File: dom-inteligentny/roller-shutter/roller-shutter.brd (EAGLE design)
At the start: 64 x 84 mm, 19 parts, among them K1 RP421110, K2 691218410003, K3 691218410003, K4 RP421110, Q1 16MHz, T1 BC847, T2 BC847, U1 ATMEGA328

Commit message: Roller shutter
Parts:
- removed K2, K3: 691218410003, Wurth_Elektronik_Electromechanic_Terminal_Blocks_Connectors_rev15c:691218410003
- added C3, C7: (no value), eagle-ltspice:C0805
- added C8, C9: (no value), eagle-ltspice:C1812
- added JP2: (no value), pinhead:1X03
- added R4, R5: (no value), eagle-ltspice:R1206
- added R6, R7: (no value), eagle-ltspice:R2512
- added X1, X4: (no value), con-ptr500:AK500/3
- added X2, X3: JST-XH-05-PIN-LONG-PAD, Rembrandt Electronics - JST XH Connectors v1-0:JST-XH-05-PACKAGE-LONG-PAD
- moved JP1 14.2 mm to (39.7, 26.7)
- moved K4 14.2 mm to (23.5, 41.1)
- moved R2 14.2 mm to (29.7, 31.5)
- moved D2 14.2 mm to (27.2, 33.8)
- moved R3 14.2 mm to (17.9, 29.2)
- moved C1 14.2 mm to (17.4, 13.0)
- moved C2 14.2 mm to (22.3, 16.0)
- moved U1 14.2 mm to (27.8, 22.6)
- moved D1 14.2 mm to (39.3, 33.5)
- moved K1 14.2 mm to (37.2, 41.1)
- moved R1 14.2 mm to (19.8, 20.8)
- moved T1 14.2 mm to (35.5, 32.4)
- moved T2 14.2 mm to (20.7, 31.7)
- moved C6 14.2 mm to (27.6, 29.1)
- moved Q1 13.7 mm to (38.5, 17.4)
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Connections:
- new net N$10: C9.2, R6.1
- new net N$9: C8.2, R7.1
- net A2: now also C7.2, R5.1, X4.3
- net A3: now also C3.2, R4.1, X4.2
- net A4: now also X2.2, X3.2
- net A5: now also X2.1, X3.1
- net GND: now also C3.1, C7.1, X2.4, X2.5, X3.4, X3.5, X4.1
- net N$1: now also JP2.1
- net N$2: now also JP2.2
- net N$4: now also C8.1, C9.1, X1.1; no longer K3.1
- net N$7: now also R7.2, X1.3; no longer K3.3
- net N$8: now also R6.2, X1.2; no longer K3.2
- net VCC: now also JP2.3, R4.2, R5.2, X2.3, X3.3
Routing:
- net GND: track 98.7 -> 218.7 mm, vias 3 -> 4
- net VCC: track 61.9 -> 176.9 mm, vias 0 -> 1
- net A3: track 0.00 -> 79.1 mm
- net A2: track 0.00 -> 73.3 mm
- net N$4: track 46.7 -> 98.5 mm
- net A4: track 0.00 -> 47.6 mm, vias 0 -> 1
- net A5: track 0.00 -> 44.7 mm, vias 0 -> 2
- net N$7: track 18.0 -> 61.4 mm
- net N$8: track 19.3 -> 44.2 mm
- net N$1: track 11.6 -> 32.7 mm
- net N$2: track 10.3 -> 20.9 mm
- net N$9: track 0.00 -> 2.49 mm
- net N$10: track 0.00 -> 2.36 mm
- net N$44: track 17.0 -> 18.3 mm
- net N$43: track 12.7 -> 12.1 mm
- added copper zone on layer 1, net GND
- added copper zone on layer 16, net GND
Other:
- board size 64 x 84 mm -> 48.5 x 84 mm
- board text added: "5V"
- board text added: "Falcon IoT Roller Shutter v1.0 weblogic.pl falcon.software"
- board text added: "GND"
- board text added: "SCL"
- board text added: "SDA"
- board text added: "VCC"

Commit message: roller shutter
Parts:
- added JP6: (no value), pinhead-zmiany-JP:3X04
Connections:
- net D10: now also JP6.2
- net D7: now also JP6.11
- net D8: now also JP6.8
- net D9: now also JP6.5
- net GND: now also JP6.12, JP6.3, JP6.6, JP6.9
- net VCC: now also JP6.1, JP6.10, JP6.4, JP6.7
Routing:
- net D10: track 0.00 -> 41.2 mm, vias 0 -> 1
- net D9: track 0.00 -> 40.7 mm, vias 0 -> 1
- net D8: track 0.00 -> 38.3 mm, vias 0 -> 1
- net D7: track 0.00 -> 36.1 mm, vias 0 -> 1
- net VCC: track 176.9 -> 207.0 mm
- net GND: track 218.7 -> 229.0 mm
- net A4: track 47.6 -> 46.9 mm
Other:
- board text added: "0"
- board text added: "1"

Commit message: Roller shutter ark change
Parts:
- removed X1: (no value), con-ptr500:AK500/3
- added X5: (no value), con-ptr500:AK500/4
- moved C8 4.62 mm to (35.9, 67.3)
- moved R7 4.62 mm to (43.2, 67.3)
- moved C9 4.36 mm to (29.3, 67.3)
- moved R6 4.24 mm to (22.1, 67.3)
- moved X4 1.52 mm to (14.4, 79.9)
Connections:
- new net N$11: C8.1, C9.1, X5.2
- net N$4: now also X5.1; no longer C8.1, C9.1, X1.1
- net N$7: now also X5.4; no longer X1.3
- net N$8: now also X5.3; no longer X1.2
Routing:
- net N$4: track 98.5 -> 77.2 mm
- net N$11: track 0.00 -> 14.7 mm
- net N$8: track 44.2 -> 42.1 mm
- net A2: track 73.3 -> 72.1 mm
- net GND: track 229.0 -> 228.4 mm
- net A3: track 79.1 -> 78.4 mm
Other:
- board text added: "A"
- board text added: "B"
- board text added: "G"
- board text added: "L"
- board text added: "L1"
- board text added: "L2"
- board text added: "N"

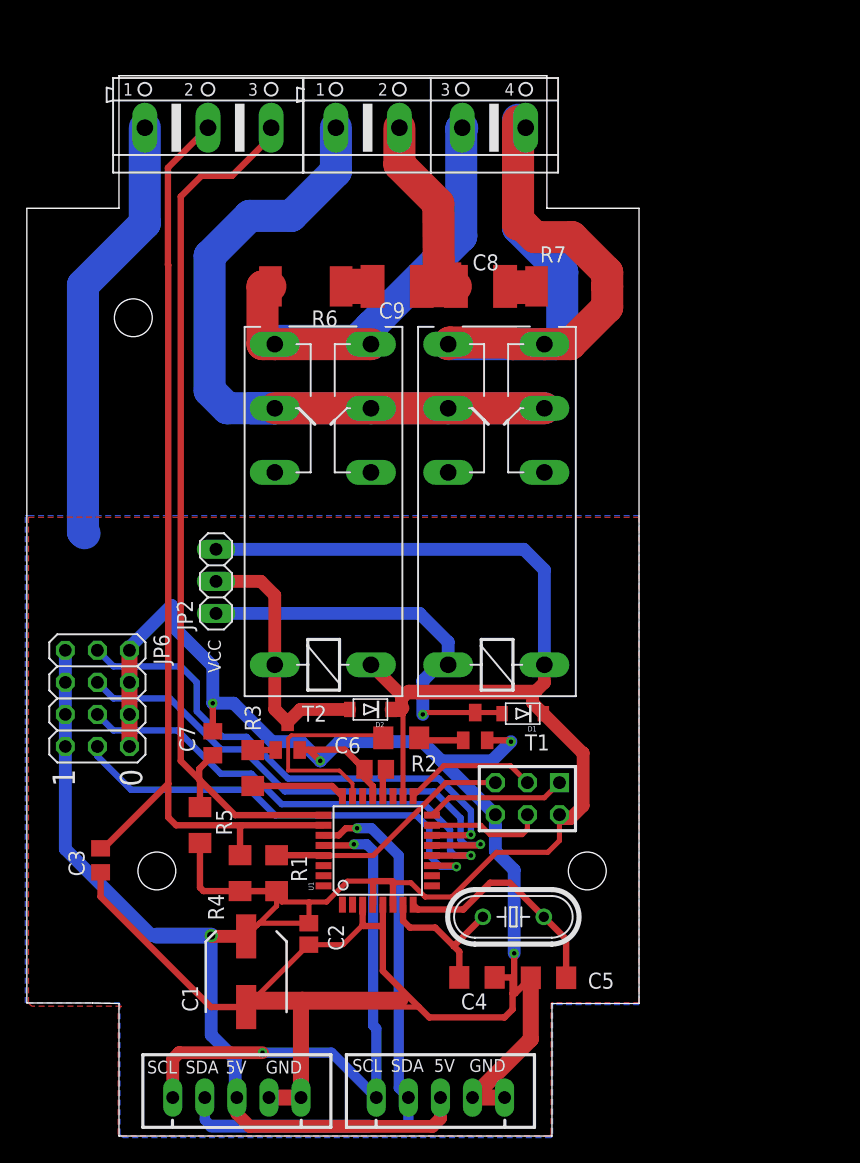
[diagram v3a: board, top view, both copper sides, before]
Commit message: Roller shutter, heat controller WIP and a new light switch input board
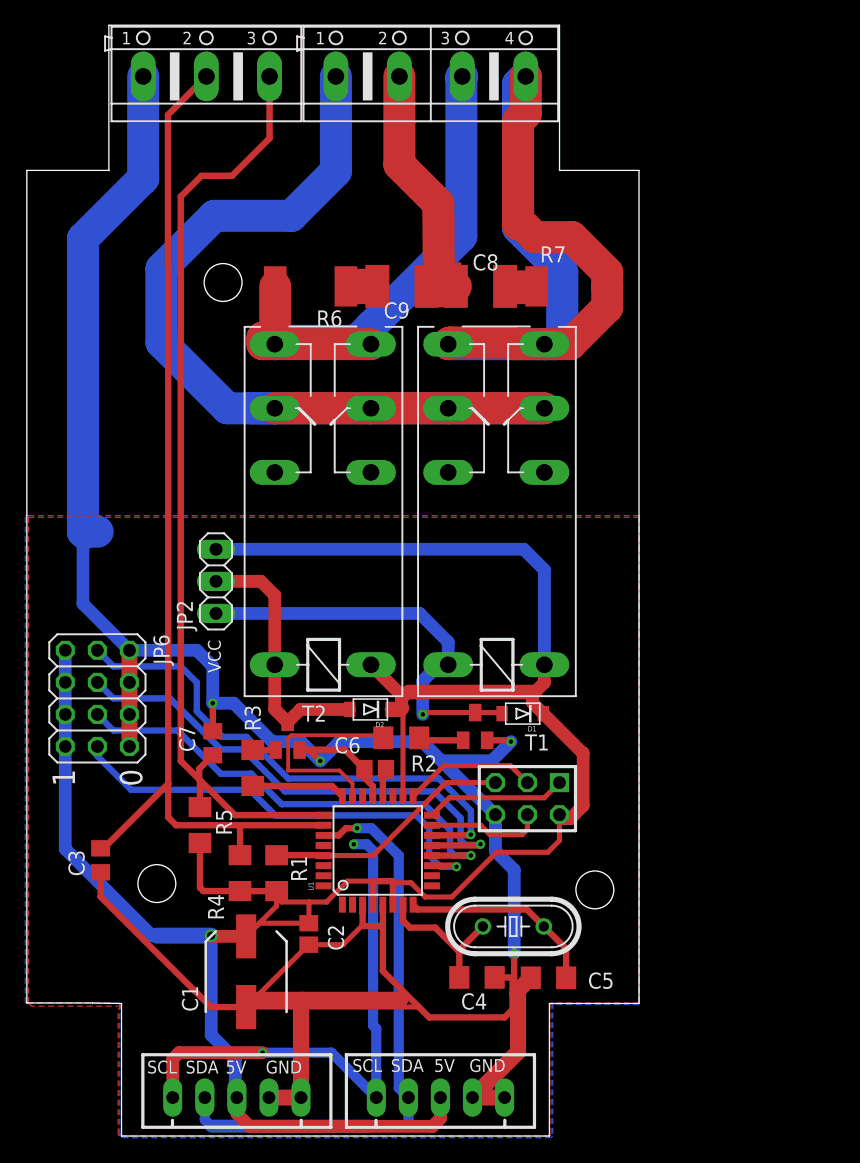
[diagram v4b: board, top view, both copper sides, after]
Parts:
- moved X4 4.07 mm to (14.2, 83.9)
- moved X5 4.06 mm to (32.0, 83.9)
- moved Q1 0.76 mm to (38.5, 16.6)
- moved C9 0.38 mm to (29.7, 67.3)
- moved R6 0.38 mm to (22.5, 67.3)
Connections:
- net A4 renamed SDA
- net A5 renamed SCL
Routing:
- net GND: track 228.4 -> 240.7 mm
- net N$4: track 77.2 -> 86.1 mm
- net N$7: track 61.6 -> 69.1 mm
- net N$8: track 42.1 -> 46.6 mm
- net N$11: track 14.7 -> 18.7 mm
- net A3: track 78.4 -> 82.4 mm
- net A2: track 72.1 -> 76.1 mm
- net SCL: track 44.7 -> 42.4 mm
- net N$44: track 18.3 -> 16.1 mm
- net N$43: track 12.1 -> 11.5 mm
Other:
- board size 48.5 x 84 mm -> 48.5 x 88 mm

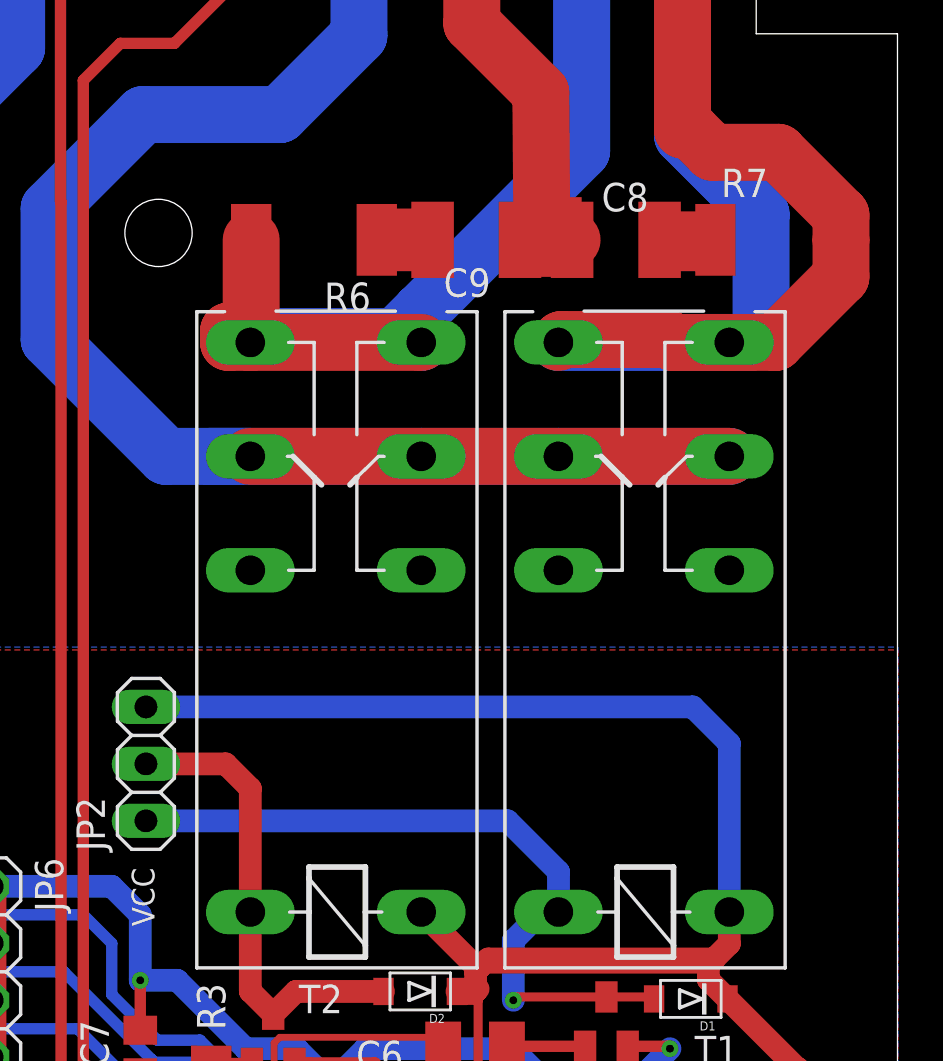
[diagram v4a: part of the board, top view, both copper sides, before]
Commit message: adds SSR to roller shutter controller
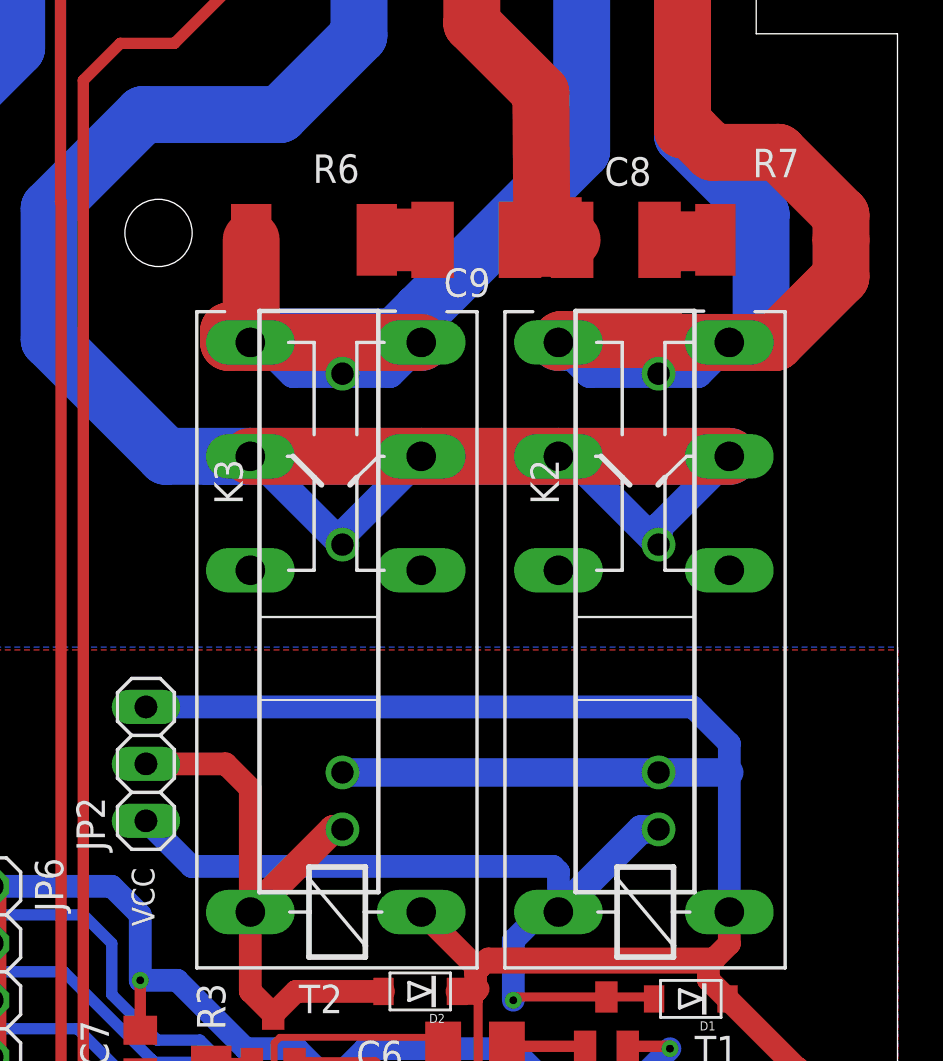
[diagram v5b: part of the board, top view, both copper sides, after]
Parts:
- added K2, K3: OMRON-G3MB-202P-SSR, Omron G3MB 202p SSR:OMRON-G3MB-202P-SSR
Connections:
- net N$1: now also K2.4
- net N$2: now also K3.4
- net N$4: now also K2.2, K3.2
- net N$7: now also K2.1
- net N$8: now also K3.1
- net VCC: now also K2.3, K3.3
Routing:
- net N$4: track 86.1 -> 108.5 mm
- net VCC: track 207.0 -> 224.3 mm
- net N$7: track 69.1 -> 77.9 mm
- net N$8: track 46.6 -> 55.2 mm
- net N$1: track 32.7 -> 38.7 mm
- net N$2: track 20.9 -> 26.6 mm
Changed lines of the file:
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@@
 <setting verticaltext="up"/>
 </settings>
-<grid distance="5" unitdist="mil" unit="mm" style="lines" multiple="1" display="no" altdistance="5" altunitdist="mil" altunit="mil"/>
+<grid distance="5" unitdist="mil" unit="mil" style="lines" multiple="1" display="no" altdistance="5" altunitdist="mil" altunit="mil"/>
 <layers>
 <layer number="1" name="Top" color="4" fill="1" visible="yes" active="yes"/>
@@
 <layer number="112" name="tSilk" color="7" fill="1" visible="yes" active="yes"/>
 <layer number="113" name="IDFDebug" color="4" fill="1" visible="yes" active="yes"/>
+<layer number="114" name="Badge_Outline" color="7" fill="1" visible="yes" active="yes"/>
+<layer number="115" name="ReferenceISLANDS" color="7" fill="1" visible="yes" active="yes"/>
 <layer number="116" name="Patch_BOT" color="9" fill="4" visible="no" active="yes"/>
 <layer number="118" name="Rect_Pads" color="7" fill="1" visible="no" active="no"/>
@@
 </element>
 <element name="R6" library="eagle-ltspice" library_urn="urn:adsk.eagle:library:217" package="R2512" package3d_urn="urn:adsk.eagle:package:13304/1" value="" x="22.479" y="67.31" smashed="yes" rot="R180">
-<attribute name="NAME" x="25.019" y="65.405" size="1.27" layer="25" rot="R180"/>
+<attribute name="NAME" x="24.511" y="71.12" size="1.27" layer="25" rot="R180"/>
 <attribute name="SPICEMODEL" value="NONE" x="22.479" y="67.31" size="1.778" layer="27" rot="R180" display="off"/>
 <attribute name="SPICEPREFIX" value="R" x="22.479" y="67.31" size="1.778" layer="27" rot="R180" display="off"/>
@@
 </element>
 <element name="R7" library="eagle-ltspice" library_urn="urn:adsk.eagle:library:217" package="R2512" package3d_urn="urn:adsk.eagle:package:13304/1" value="" x="43.18" y="67.31" smashed="yes">
-<attribute name="NAME" x="40.64" y="69.215" size="1.27" layer="25"/>
+<attribute name="NAME" x="42.037" y="70.104" size="1.27" layer="25"/>
 <attribute name="SPICEMODEL" value="NONE" x="43.18" y="67.31" size="1.778" layer="27" display="off"/>
 <attribute name="SPICEPREFIX" value="R" x="43.18" y="67.31" size="1.778" layer="27" display="off"/>
@@
 </element>
 <element name="C8" library="eagle-ltspice" library_urn="urn:adsk.eagle:library:217" package="C1812" package3d_urn="urn:adsk.eagle:package:13267/1" value="" x="35.941" y="67.31" smashed="yes">
-<attribute name="NAME" x="35.306" y="68.58" size="1.27" layer="25"/>
+<attribute name="NAME" x="35.433" y="69.723" size="1.27" layer="25"/>
 <attribute name="SPICEMODEL" value="NONE" x="35.941" y="67.31" size="1.778" layer="27" display="off"/>
 <attribute name="SPICEPREFIX" value="C" x="35.941" y="67.31" size="1.778" layer="27" display="off"/>
@@
 <attribute name="POPULARITY" value="4" x="32.004" y="83.947" size="1.778" layer="27" display="off"/>
 <attribute name="VALUE" x="21.9202" y="78.232" size="1.778" layer="27" ratio="10"/>
+</element>
+<element name="K2" library="Omron G3MB 202p SSR" package="OMRON-G3MB-202P-SSR" value="OMRON-G3MB-202P-SSR" x="37.846" y="48.641" smashed="yes" rot="R270">
+<attribute name="MF" value="" x="37.846" y="48.641" size="1.778" layer="27" rot="R270" display="off"/>
+<attribute name="MPN" value="" x="37.846" y="48.641" size="1.778" layer="27" rot="R270" display="off"/>
+<attribute name="NAME" x="32.131" y="57.531" size="1.27" layer="25" rot="R270"/>
+<attribute name="OC_FARNELL" value="" x="37.846" y="48.641" size="1.778" layer="27" rot="R270" display="off"/>
+<attribute name="OC_NEWARK" value="" x="37.846" y="48.641" size="1.778" layer="27" rot="R270" display="off"/>
+</element>
+<element name="K3" library="Omron G3MB 202p SSR" package="OMRON-G3MB-202P-SSR" value="OMRON-G3MB-202P-SSR" x="23.749" y="48.641" smashed="yes" rot="R270">
+<attribute name="MF" value="" x="23.749" y="48.641" size="1.778" layer="27" rot="R270" display="off"/>
+<attribute name="MPN" value="" x="23.749" y="48.641" size="1.778" layer="27" rot="R270" display="off"/>
+<attribute name="NAME" x="18.034" y="57.531" size="1.27" layer="25" rot="R270"/>
+<attribute name="OC_FARNELL" value="" x="23.749" y="48.641" size="1.778" layer="27" rot="R270" display="off"/>
+<attribute name="OC_NEWARK" value="" x="23.749" y="48.641" size="1.778" layer="27" rot="R270" display="off"/>
 </element>
 </elements>
@@
 <contactref element="JP2" pad="3"/>
 <wire x1="14.986" y1="46.482" x2="39.37" y2="46.482" width="1.016" layer="16"/>
-<wire x1="41.001" y1="44.851" x2="41.001" y2="37.335" width="1.016" layer="16"/>
+<wire x1="41.001" y1="44.851" x2="41.001" y2="43.561" width="1.016" layer="16"/>
+<wire x1="41.001" y1="43.561" x2="41.001" y2="37.335" width="1.016" layer="16"/>
 <wire x1="39.37" y1="46.482" x2="41.001" y2="44.851" width="1.016" layer="16"/>
 <wire x1="17.653" y1="0.762" x2="32.131" y2="0.762" width="1.016" layer="1"/>
@@
 <wire x1="3.048" y1="33.401" x2="3.048" y2="35.941" width="1.016" layer="16"/>
 <wire x1="3.048" y1="35.941" x2="3.048" y2="38.481" width="1.016" layer="16"/>
+<contactref element="K2" pad="3"/>
+<contactref element="K3" pad="3"/>
+<wire x1="23.749" y1="43.561" x2="37.846" y2="43.561" width="1.27" layer="16"/>
+<wire x1="37.846" y1="43.561" x2="41.001" y2="43.561" width="1.27" layer="16"/>
 <wire x1="40.9205" y1="33.461" x2="40.322503125" y2="35.242503125" width="0" layer="19" extent="1-1"/>
 <wire x1="29.001" y1="18.3274" x2="29.001003125" y2="20.147996875" width="0" layer="19" extent="1-1"/>
@@
 <wire x1="31.369" y1="36.068" x2="31.369" y2="33.401" width="1.016" layer="16"/>
 <contactref element="JP2" pad="1"/>
-<wire x1="14.986" y1="41.402" x2="31.115" y2="41.402" width="1.016" layer="16"/>
+<wire x1="33.147" y1="39.37" x2="17.018" y2="39.37" width="1.016" layer="16"/>
+<wire x1="14.986" y1="41.402" x2="17.018" y2="39.37" width="1.016" layer="16"/>
 <wire x1="33.381" y1="39.136" x2="33.381" y2="37.335" width="1.016" layer="16"/>
-<wire x1="31.115" y1="41.402" x2="33.381" y2="39.136" width="1.016" layer="16"/>
+<wire x1="33.147" y1="39.37" x2="33.381" y2="39.136" width="1.016" layer="16"/>
+<contactref element="K2" pad="4"/>
+<wire x1="33.381" y1="37.335" x2="37.067" y2="41.021" width="1.27" layer="16"/>
+<wire x1="37.067" y1="41.021" x2="37.846" y2="41.021" width="1.27" layer="16"/>
 </signal>
 <signal name="N$2">
@@
 <wire x1="18.542" y1="43.942" x2="14.986" y2="43.942" width="1.016" layer="1"/>
 <wire x1="19.641" y1="42.843" x2="18.542" y2="43.942" width="1.016" layer="1"/>
+<contactref element="K3" pad="4"/>
+<wire x1="19.641" y1="37.335" x2="23.327" y2="41.021" width="1.27" layer="1"/>
+<wire x1="23.327" y1="41.021" x2="23.749" y2="41.021" width="1.27" layer="1"/>
 </signal>
 <signal name="N$5">
@@
 <wire x1="24.4856" y1="76.4286" x2="24.4856" y2="83.947" width="2.54" layer="16"/>
 <wire x1="20.955" y1="72.898" x2="24.4856" y2="76.4286" width="2.54" layer="16"/>
+<contactref element="K3" pad="2"/>
+<contactref element="K2" pad="2"/>
+<wire x1="23.749" y1="53.721" x2="19.815" y2="57.655" width="1.27" layer="16"/>
+<wire x1="19.815" y1="57.655" x2="19.641" y2="57.655" width="1.27" layer="16"/>
+<wire x1="23.749" y1="53.721" x2="23.749" y2="54.143" width="1.27" layer="16"/>
+<wire x1="23.749" y1="54.143" x2="27.261" y2="57.655" width="1.27" layer="16"/>
+<wire x1="37.846" y1="53.721" x2="33.912" y2="57.655" width="1.27" layer="16"/>
+<wire x1="33.912" y1="57.655" x2="33.381" y2="57.655" width="1.27" layer="16"/>
+<wire x1="37.846" y1="53.721" x2="37.846" y2="54.5" width="1.27" layer="16"/>
+<wire x1="37.846" y1="54.5" x2="41.001" y2="57.655" width="1.27" layer="16"/>
 </signal>
 <signal name="N$7">
@@
 <wire x1="39.5224" y1="83.947" x2="38.914" y2="83.3386" width="2.54" layer="16"/>
 <wire x1="38.914" y1="83.3386" x2="38.914" y2="71.957" width="2.54" layer="16"/>
+<contactref element="K2" pad="1"/>
+<wire x1="37.846" y1="61.341" x2="34.775" y2="61.341" width="1.27" layer="16"/>
+<wire x1="34.775" y1="61.341" x2="33.381" y2="62.735" width="1.27" layer="16"/>
+<wire x1="37.846" y1="61.341" x2="39.607" y2="61.341" width="1.27" layer="16"/>
+<wire x1="39.607" y1="61.341" x2="41.001" y2="62.735" width="1.27" layer="16"/>
 </signal>
 <signal name="N$8">
@@
 <wire x1="19.679" y1="67.31" x2="19.679" y2="63.246" width="2.54" layer="1"/>
 <wire x1="19.679" y1="63.246" x2="18.669" y2="63.246" width="2.54" layer="1"/>
+<contactref element="K3" pad="1"/>
+<wire x1="23.749" y1="61.341" x2="21.549" y2="61.341" width="1.27" layer="16"/>
+<wire x1="21.549" y1="61.341" x2="19.898" y2="62.992" width="1.27" layer="16"/>
+<wire x1="23.749" y1="61.341" x2="25.867" y2="61.341" width="1.27" layer="16"/>
+<wire x1="25.867" y1="61.341" x2="27.261" y2="62.735" width="1.27" layer="16"/>
 </signal>
 <signal name="N$9">
